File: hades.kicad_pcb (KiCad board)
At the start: 2 copper layers, 63.2 x 38.5 mm, 25 parts, among them J1 USB_B_Micro, J3 outgooing water temperature, J4 incomming water temperature, J5 Outside temperature, J6 Relay, Q1 2N2222, SW1 reset, SW2 mode switch, U1 LM1117MPX-3_3_NOPB, U2 ESP32-WROOM-32D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

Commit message: bugfix: on board temperature sensor connected to the other one wire devices
bufix: The on board temperature sensor wasn't connected to the correct one wire bus
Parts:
- J2: renamed from Programming Header
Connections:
- U2 pad 10: Net-(U2-Pad10) -> (no net)
- U3 pad 2: Net-(U2-Pad10) -> Net-(J3-Pad2)
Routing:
- net Net-(U2-Pad10): track 49.0 -> 0.00 mm, vias 3 -> 0
- net Net-(J3-Pad2): track 84.7 -> 111.4 mm
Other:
- board text added: "Hades Poolcontroller V1.1"
- board text removed: "Poolcontroller V1"

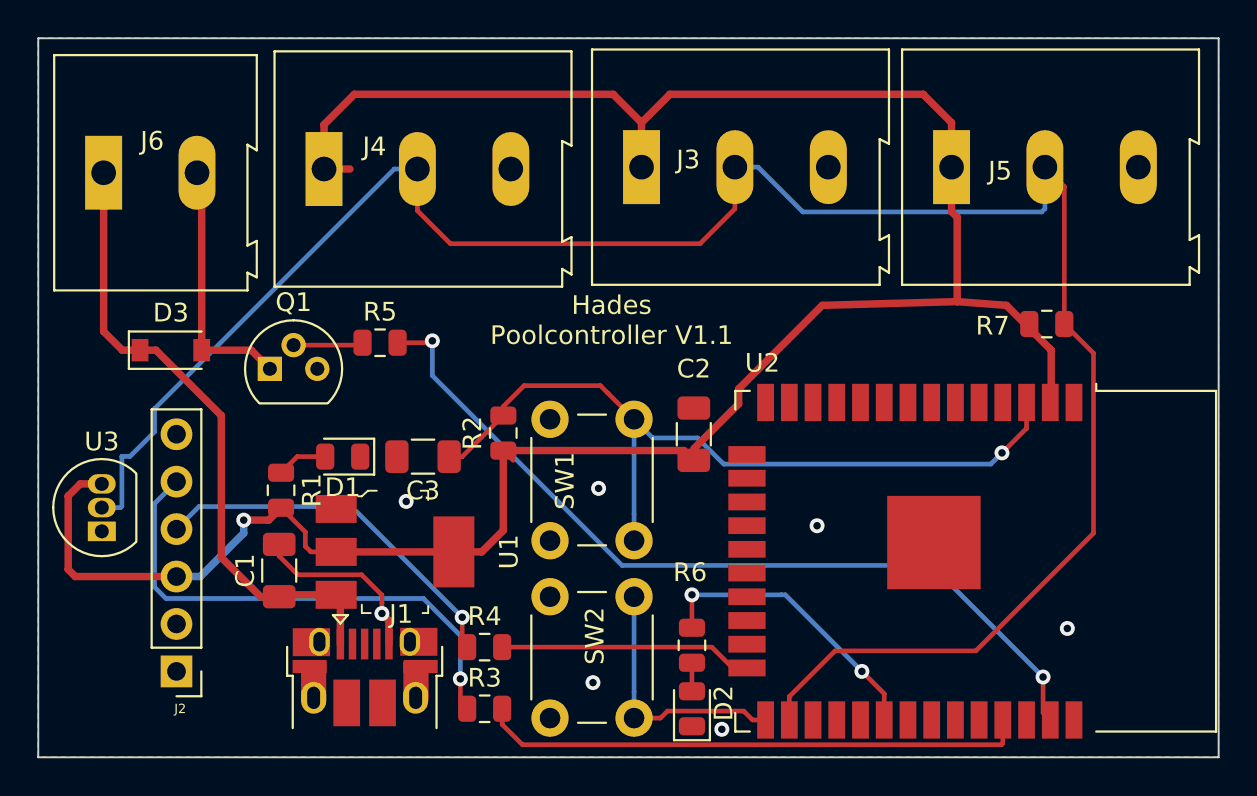
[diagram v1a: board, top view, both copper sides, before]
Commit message: fixed wrong connection to rx pin
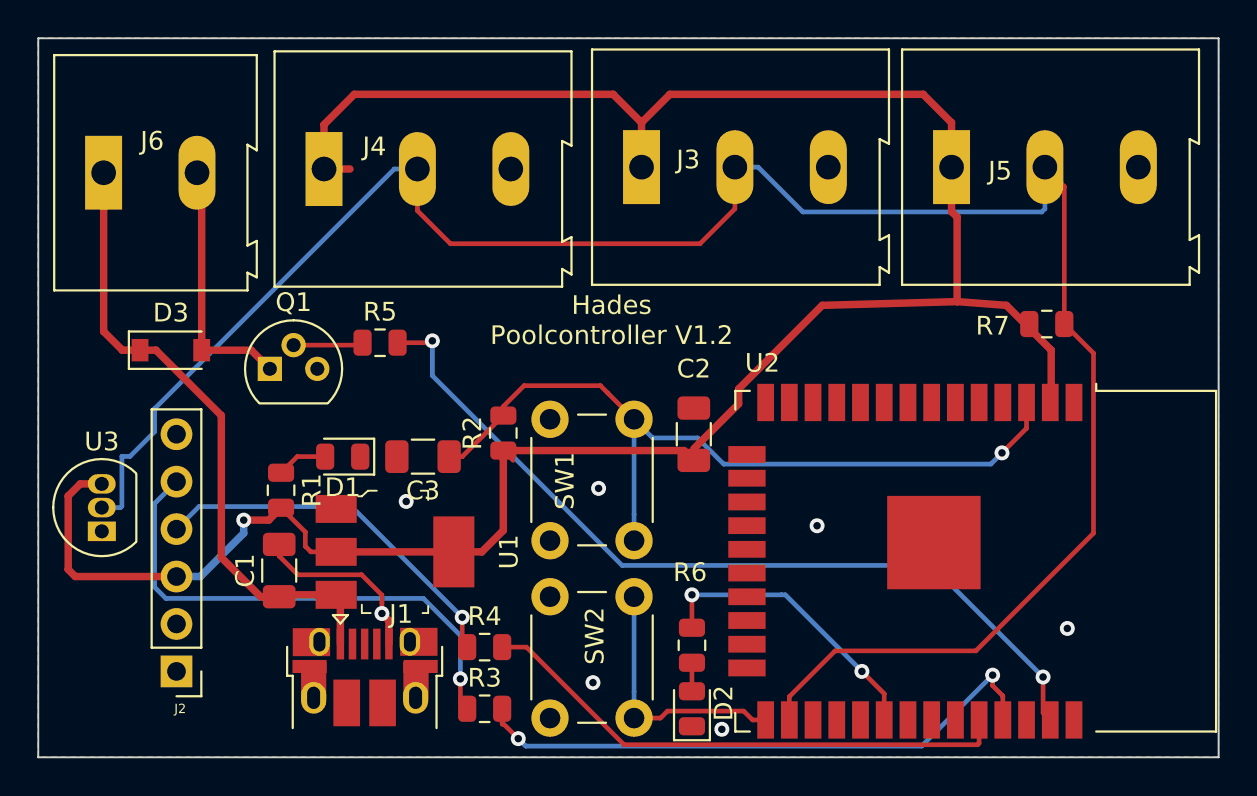
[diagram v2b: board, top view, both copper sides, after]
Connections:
- U2 pad 24: Net-(R4-Pad2) -> (no net)
- U2 pad 34: (no net) -> Net-(R4-Pad2)
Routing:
- net Net-(R4-Pad2): track 13.6 -> 29.0 mm
- net Net-(R3-Pad2): track 29.4 -> 32.8 mm, vias 0 -> 2
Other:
- board text added: "Hades Poolcontroller V1.2"
- board text removed: "Hades Poolcontroller V1.1"
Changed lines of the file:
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@@
     (thickness 1.6)
     (drawings 5)
-    (tracks 180)
+    (tracks 190)
     (zones 0)
     (modules 25)
@@
     (title "Hades pool heater controller")
     (date 2020-05-06)
-    (rev 1.1)
+    (rev 1.2)
     (comment 4 "Author: Vincent Mangelschots")
   )
@@
     (pad 22 smd rect (at 3.175 9.255) (size 2 0.9) (layers F.Cu F.Paste F.Mask))
     (pad 23 smd rect (at 4.445 9.255) (size 2 0.9) (layers F.Cu F.Paste F.Mask))
-    (pad 24 smd rect (at 5.715 9.255) (size 2 0.9) (layers F.Cu F.Paste F.Mask)
-      (net 7 "Net-(R4-Pad2)"))
+    (pad 24 smd rect (at 5.715 9.255) (size 2 0.9) (layers F.Cu F.Paste F.Mask))
     (pad 25 smd rect (at 8.5 8.255 270) (size 2 0.9) (layers F.Cu F.Paste F.Mask)
       (net 8 "Net-(SW2-Pad1)"))
@@
     (pad 32 smd rect (at 8.5 -0.635 270) (size 2 0.9) (layers F.Cu F.Paste F.Mask))
     (pad 33 smd rect (at 8.5 -1.905 270) (size 2 0.9) (layers F.Cu F.Paste F.Mask))
-    (pad 34 smd rect (at 8.5 -3.175 270) (size 2 0.9) (layers F.Cu F.Paste F.Mask))
+    (pad 34 smd rect (at 8.5 -3.175 270) (size 2 0.9) (layers F.Cu F.Paste F.Mask)
+      (net 7 "Net-(R4-Pad2)"))
     (pad 35 smd rect (at 8.5 -4.445 270) (size 2 0.9) (layers F.Cu F.Paste F.Mask)
       (net 6 "Net-(R3-Pad2)"))
@@
     )
   )
-  (gr_text "Hades\nPoolcontroller V1.1\n" (at 135.4 37) (layer F.SilkS)
+  (gr_text "Hades\nPoolcontroller V1.2\n" (at 135.4 37) (layer F.SilkS)
     (effects (font (size 1 1) (thickness 0.15)))
   )
@@
   (segment (start 117.7 45.1625) (end 118.5625 44.3) (width 0.25) (layer F.Cu) (net 4) (status 10))
   (segment (start 129.5375 57.8) (end 129.5375 58.6375) (width 0.25) (layer F.Cu) (net 6) (status 10))
-  (segment (start 156.345 59.65) (end 156.345 58.4) (width 0.25) (layer F.Cu) (net 6) (status 20))
-  (segment (start 156.269999 59.725001) (end 156.345 59.65) (width 0.25) (layer F.Cu) (net 6))
-  (segment (start 129.5375 58.6375) (end 130.625001 59.725001) (width 0.25) (layer F.Cu) (net 6))
-  (segment (start 130.625001 59.725001) (end 156.269999 59.725001) (width 0.25) (layer F.Cu) (net 6))
-  (segment (start 141.879998 55.615) (end 142.645 55.615) (width 0.25) (layer F.Cu) (net 7) (status 30))
-  (segment (start 140.764998 54.5) (end 141.879998 55.615) (width 0.25) (layer F.Cu) (net 7) (status 20))
-  (segment (start 129.5375 54.5) (end 140.764998 54.5) (width 0.25) (layer F.Cu) (net 7) (status 10))
+  (segment (start 129.5375 57.8) (end 129.8 57.8) (width 0.25) (layer F.Cu) (net 6))
+  (via (at 130.4 59.4) (size 0.8) (drill 0.4) (layers F.Cu B.Cu) (net 6))
+  (segment (start 129.5375 57.8) (end 129.5375 58.5375) (width 0.25) (layer F.Cu) (net 6))
+  (segment (start 129.5375 58.5375) (end 130.4 59.4) (width 0.25) (layer F.Cu) (net 6))
+  (segment (start 152.000001 59.799999) (end 155.8 56) (width 0.25) (layer B.Cu) (net 6))
+  (segment (start 130.4 59.4) (end 130.799999 59.799999) (width 0.25) (layer B.Cu) (net 6))
+  (via (at 155.8 56) (size 0.8) (drill 0.4) (layers F.Cu B.Cu) (net 6))
+  (segment (start 130.799999 59.799999) (end 152.000001 59.799999) (width 0.25) (layer B.Cu) (net 6))
+  (segment (start 156.345 57.15) (end 156.345 58.4) (width 0.25) (layer F.Cu) (net 6))
+  (segment (start 156.345 57.110685) (end 156.345 57.15) (width 0.25) (layer F.Cu) (net 6))
+  (segment (start 155.8 56.565685) (end 156.345 57.110685) (width 0.25) (layer F.Cu) (net 6))
+  (segment (start 155.8 56) (end 155.8 56.565685) (width 0.25) (layer F.Cu) (net 6))
+  (segment (start 154.999999 59.725001) (end 155.075 59.65) (width 0.25) (layer F.Cu) (net 7))
+  (segment (start 136.063999 59.725001) (end 154.999999 59.725001) (width 0.25) (layer F.Cu) (net 7))
+  (segment (start 155.075 59.65) (end 155.075 58.4) (width 0.25) (layer F.Cu) (net 7))
+  (segment (start 130.838998 54.5) (end 136.063999 59.725001) (width 0.25) (layer F.Cu) (net 7))
+  (segment (start 129.5375 54.5) (end 130.838998 54.5) (width 0.25) (layer F.Cu) (net 7))
   (segment (start 138.014213 58.3) (end 136.6 58.3) (width 0.25) (layer F.Cu) (net 8) (status 20))
   (segment (start 138.389223 57.92499) (end 138.014213 58.3) (width 0.25) (layer F.Cu) (net 8))
@@
   (segment (start 144.5 51.7) (end 144.7 51.7) (width 0.25) (layer B.Cu) (net 15))
   (segment (start 144.7 51.7) (end 148.8 55.8) (width 0.25) (layer B.Cu) (net 15))
-  (segment (start 149.995 56.995) (end 149.995 58.4) (width 0.25) (layer F.Cu) (net 15))
+  (segment (start 149.995 56.995) (end 149.995 58.4) (width 0.25) (layer F.Cu) (net 15) (status 20))
   (segment (start 148.8 55.8) (end 149.995 56.995) (width 0.25) (layer F.Cu) (net 15))
-  (segment (start 109.17501 46.95499) (end 109.1 47.03) (width 0.25) (layer B.Cu) (net 17))
-  (segment (start 109.1 47.03) (end 108.1 47.03) (width 0.25) (layer B.Cu) (net 17) (status 20))
   (segment (start 113.35 29.25) (end 113.2 29.1) (width 0.4) (layer F.Cu) (net 16) (status 30))
   (segment (start 113.45 29.35) (end 113.2 29.1) (width 0.4) (layer F.Cu) (net 16) (status 30))
@@
   (segment (start 116.1 38.6) (end 117.1 39.6) (width 0.4) (layer F.Cu) (net 16) (status 20))
   (segment (start 113.45 38.6) (end 116.1 38.6) (width 0.4) (layer F.Cu) (net 16) (status 10))
+  (segment (start 109.17501 46.95499) (end 109.1 47.03) (width 0.25) (layer B.Cu) (net 17))
+  (segment (start 109.1 47.03) (end 108.1 47.03) (width 0.25) (layer B.Cu) (net 17) (status 20))
   (segment (start 125 31.13) (end 126.77 32.9) (width 0.25) (layer F.Cu) (net 17))
   (segment (start 125 28.9) (end 125 31.13) (width 0.25) (layer F.Cu) (net 17) (status 10))
@@
   (segment (start 161.2 48.4) (end 161.2 38.7625) (width 0.25) (layer F.Cu) (net 17))
   (segment (start 109.17501 44.285988) (end 109.17501 46.95499) (width 0.25) (layer B.Cu) (net 17))
-  (segment (start 123.76 28.9) (end 125 28.9) (width 0.25) (layer B.Cu) (net 17))
+  (segment (start 123.76 28.9) (end 125 28.9) (width 0.25) (layer B.Cu) (net 17) (status 20))
   (segment (start 110.924999 41.735001) (end 123.76 28.9) (width 0.25) (layer B.Cu) (net 17))
   (segment (start 110.924999 42.975001) (end 110.924999 41.735001) (width 0.25) (layer B.Cu) (net 17))

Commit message: the bjt for the relay was connected to a input only pin
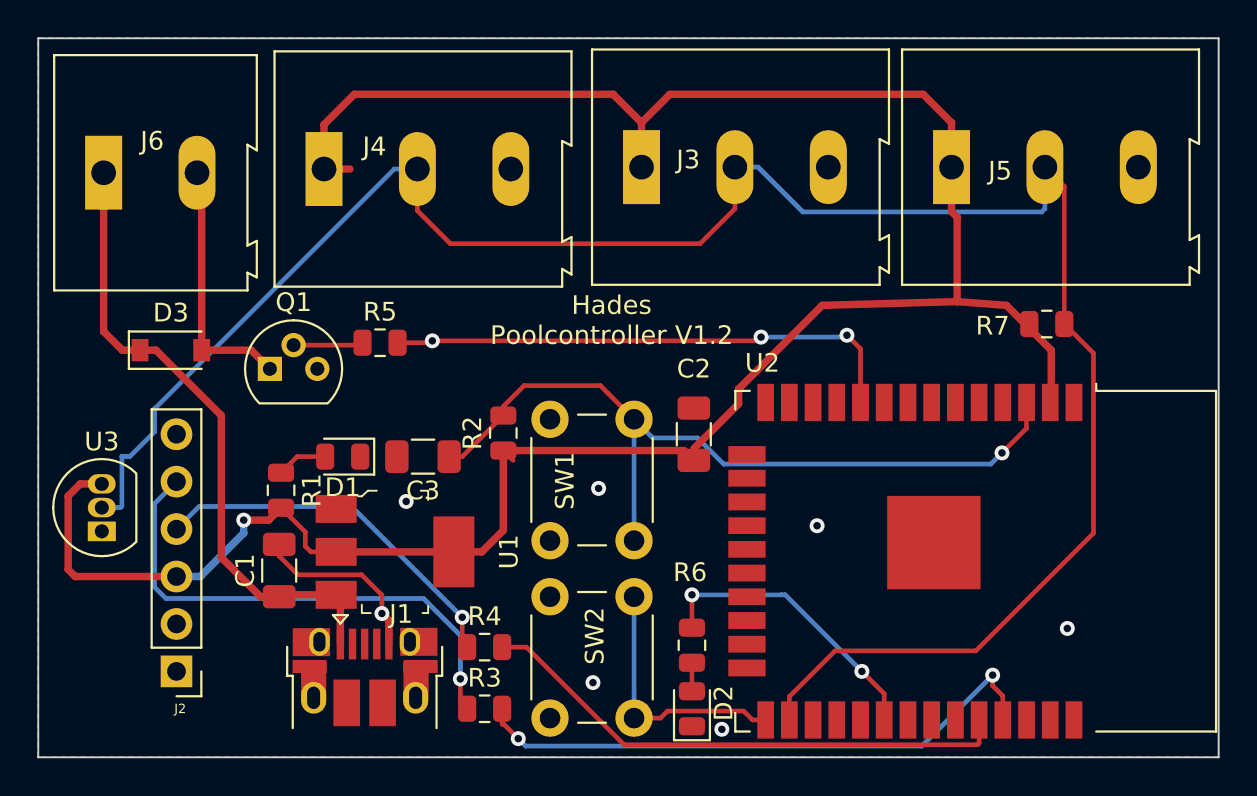
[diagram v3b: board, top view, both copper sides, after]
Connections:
- U2 pad 10: (no net) -> Net-(R5-Pad2)
- U2 pad 37: Net-(R5-Pad2) -> (no net)
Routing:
- net Net-(R5-Pad2): track 45.6 -> 28.1 mm, vias 2 -> 3
